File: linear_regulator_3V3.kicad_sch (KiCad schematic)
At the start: 3 parts, among them U23 NCP1117-3.3_SOT223

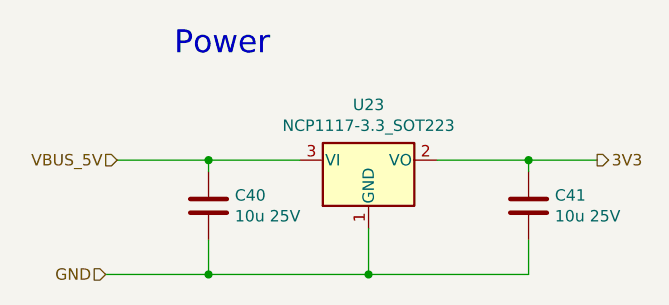
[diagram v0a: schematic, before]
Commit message: Refactored top sheet
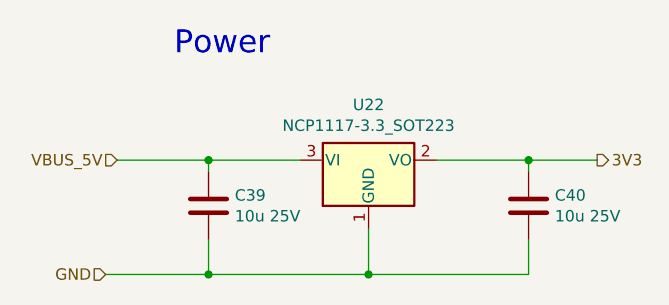
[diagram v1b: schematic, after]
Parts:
- renumbered C40 to C39, C41 to C40, U23 to U22
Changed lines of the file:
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@@
   (symbol (lib_id "Device:C") (at 100.33 41.91 0) (unit 1)
     (in_bom yes) (on_board yes)
-    (property "Reference" "C40" (id 0) (at 103.251 40.7416 0)
+    (property "Reference" "C39" (id 0) (at 103.251 40.7416 0)
       (effects (font (size 1.27 1.27)) (justify left))
     )
@@
   (symbol (lib_id "Device:C") (at 135.89 41.91 0) (unit 1)
     (in_bom yes) (on_board yes)
-    (property "Reference" "C41" (id 0) (at 138.811 40.7416 0)
+    (property "Reference" "C40" (id 0) (at 138.811 40.7416 0)
       (effects (font (size 1.27 1.27)) (justify left))
     )
@@
   (symbol (lib_id "Regulator_Linear:NCP1117-3.3_SOT223") (at 118.11 36.83 0) (unit 1)
     (in_bom yes) (on_board yes)
-    (property "Reference" "U23" (id 0) (at 118.11 30.6832 0))
+    (property "Reference" "U22" (id 0) (at 118.11 30.6832 0))
     (property "Value" "NCP1117-3.3_SOT223" (id 1) (at 118.11 32.9946 0))
     (property "Footprint" "Package_TO_SOT_SMD:SOT-223-3_TabPin2" (id 2) (at 118.11 31.75 0)
